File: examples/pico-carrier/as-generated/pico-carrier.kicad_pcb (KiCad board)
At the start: 2 copper layers, 82 x 68 mm, 9 parts, among them J1 5V IN, J3 GP0-GP15, J4 GP16-GP28, PWR, U1 Pico

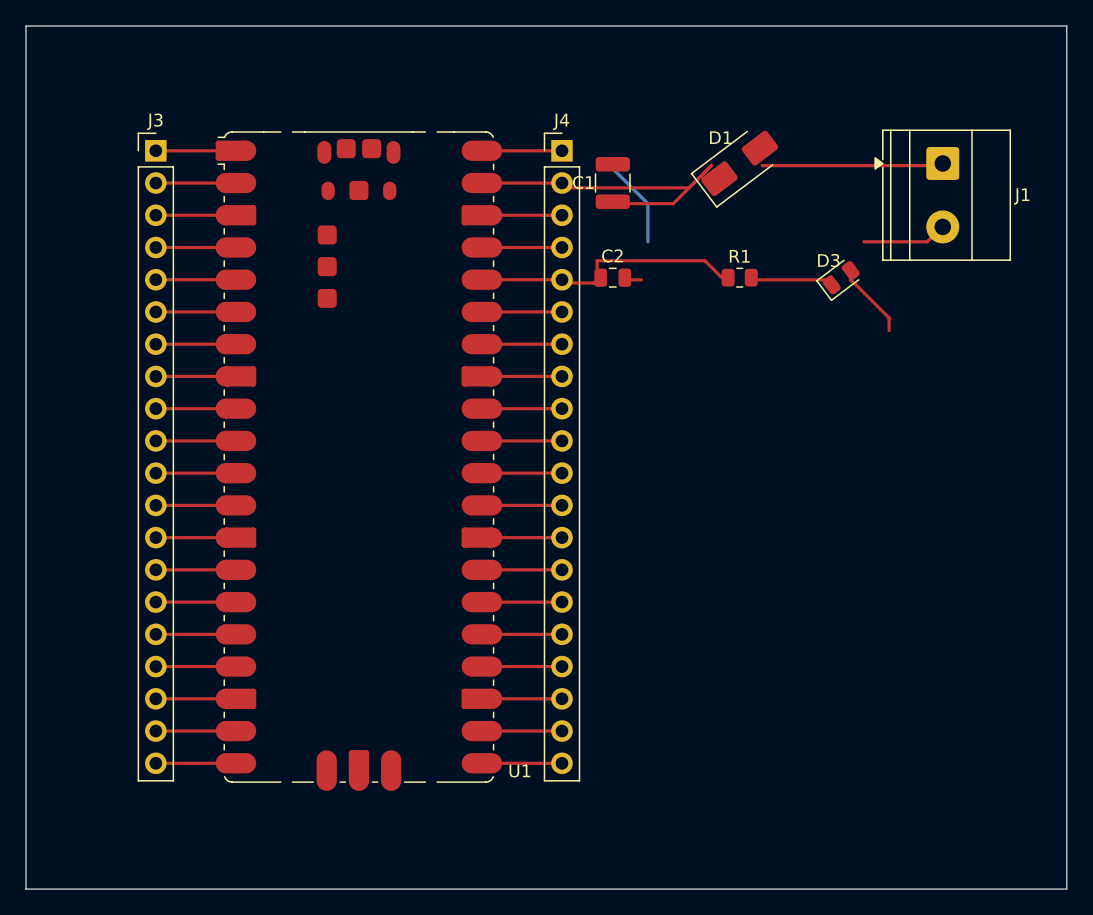
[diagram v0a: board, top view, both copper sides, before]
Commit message: Regenerate the five as round three drew them
All five reviewed projects pass their gates again: the buck all wire
with its feedback drawn home, the motor's logic named at the header,
the carrier reading as the pinout table it is - with its feed diode
finally pointing the right way - the filter compact with test points,
and the FPGA's capacitors sitting beside the units they feed. Thirty
renders redrawn, verdict tables at today's numbers.

Co-Authored-By: Claude Fable 5 <noreply@anthropic.com>
Claude-Session: https://claude.ai/code/session_01DUj7Ltu92tWg159mCSacwY
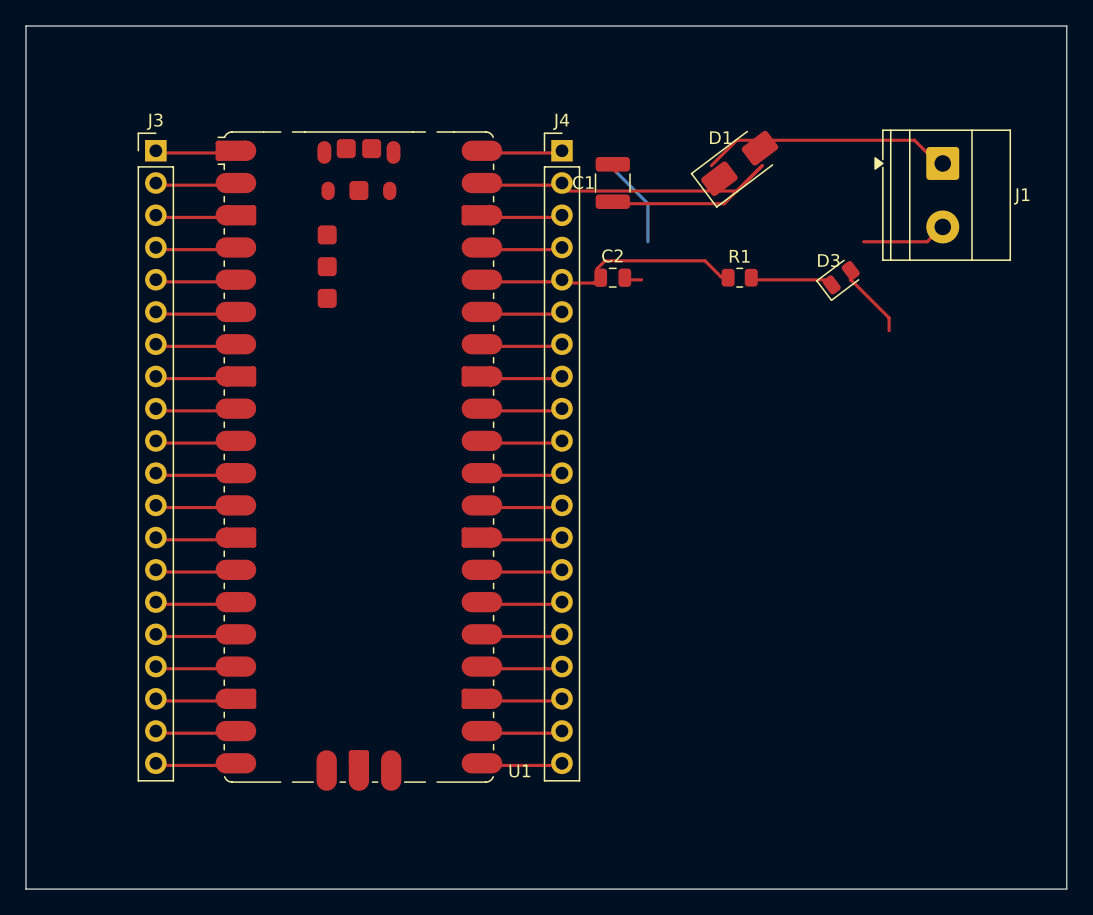
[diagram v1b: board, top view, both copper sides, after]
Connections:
- D1 pad 1: +5V -> /VSYS
- D1 pad 2: /VSYS -> +5V
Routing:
- net /VSYS: track 28.4 -> 36.6 mm
- net +5V: track 14.0 -> 19.7 mm

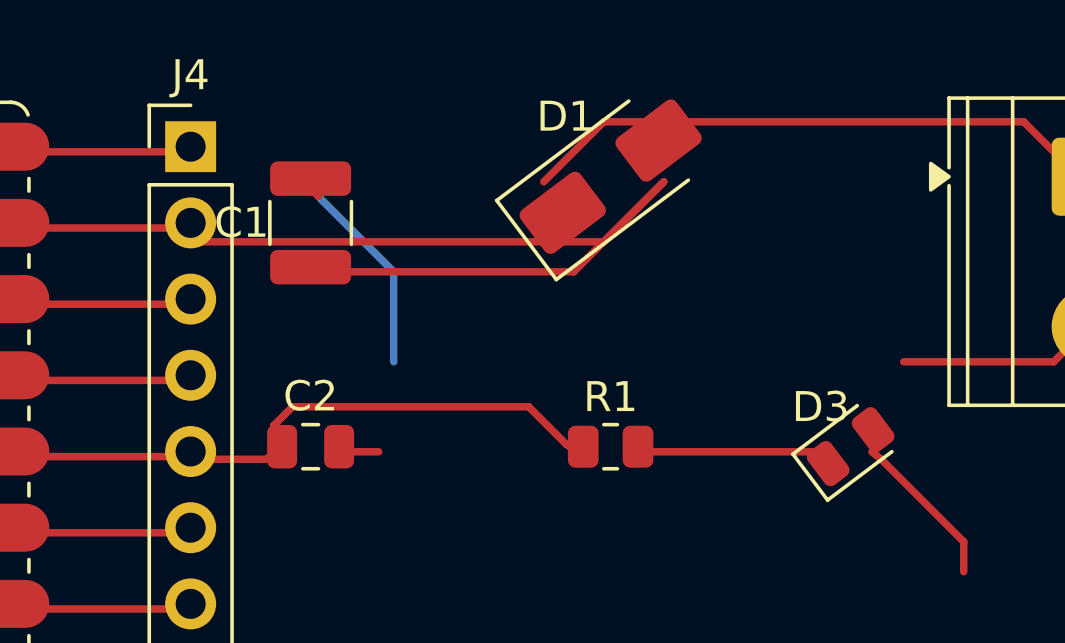
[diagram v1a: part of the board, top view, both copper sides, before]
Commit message: Regenerate the four boards whose corners were off the grid
Ninety-one bends at angles nobody chose, now none. All four still pass
their gates.

Co-Authored-By: Claude Fable 5 <noreply@anthropic.com>
Claude-Session: https://claude.ai/code/session_01DUj7Ltu92tWg159mCSacwY
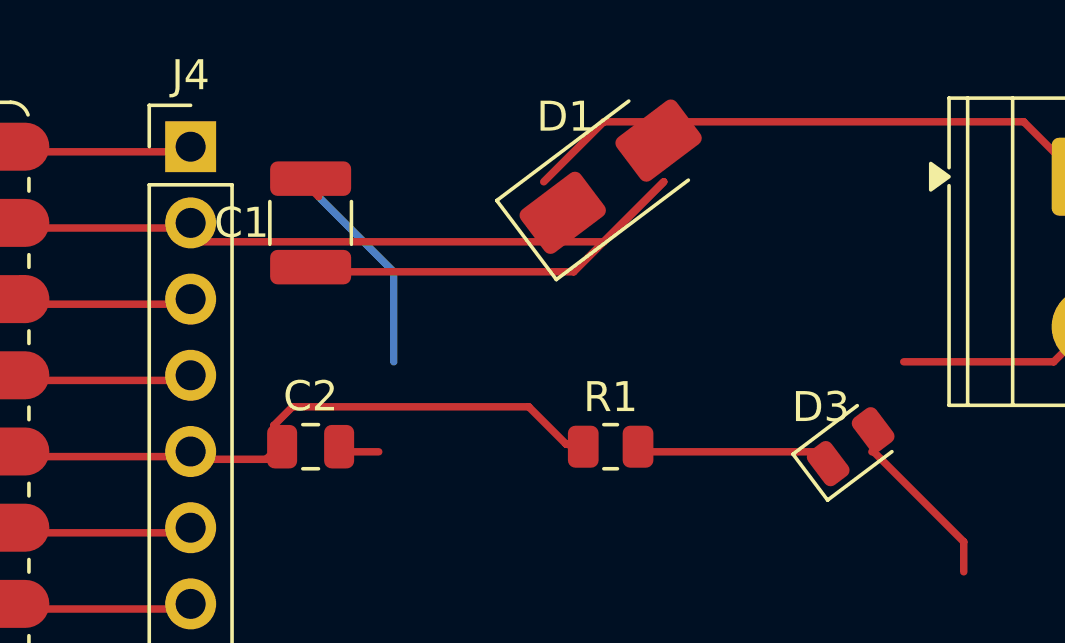
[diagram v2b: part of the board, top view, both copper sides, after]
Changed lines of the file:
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@@
 	(segment (start 156.0 73.0) (end 142.5 73.0) (width 0.25) (layer "F.Cu") (net 36))
 	(segment (start 142.5 73.0) (end 142.25 72.75) (width 0.25) (layer "F.Cu") (net 36))
-	(segment (start 142.25 72.75) (end 142.0 72.54) (width 0.25) (layer "F.Cu") (net 36))
-	(segment (start 146.0 74.015) (end 146.25 74.0) (width 0.25) (layer "F.Cu") (net 36))
+	(segment (start 142.25 72.75) (end 142.21 72.75) (width 0.25) (layer "F.Cu") (net 36))
+	(segment (start 142.21 72.75) (end 142.0 72.54) (width 0.25) (layer "F.Cu") (net 36))
+	(segment (start 146.0 74.015) (end 146.235 74.015) (width 0.25) (layer "F.Cu") (net 36))
+	(segment (start 146.235 74.015) (end 146.25 74.0) (width 0.25) (layer "F.Cu") (net 36))
 	(segment (start 146.25 74.0) (end 155.0 74.0) (width 0.25) (layer "F.Cu") (net 36))
 	(segment (start 155.0 74.0) (end 158.0 71.0) (width 0.25) (layer "F.Cu") (net 36))
-	(segment (start 145.05 80.0) (end 144.75 80.25) (width 0.25) (layer "F.Cu") (net 2))
+	(segment (start 145.05 80.0) (end 145.0 80.0) (width 0.25) (layer "F.Cu") (net 2))
+	(segment (start 145.0 80.0) (end 144.75 80.25) (width 0.25) (layer "F.Cu") (net 2))
 	(segment (start 144.75 80.25) (end 142.25 80.25) (width 0.25) (layer "F.Cu") (net 2))
-	(segment (start 142.25 80.25) (end 142.0 80.16) (width 0.25) (layer "F.Cu") (net 2))
-	(segment (start 145.05 80.0) (end 145.0 79.75) (width 0.25) (layer "F.Cu") (net 2))
+	(segment (start 142.25 80.25) (end 142.09 80.25) (width 0.25) (layer "F.Cu") (net 2))
+	(segment (start 142.09 80.25) (end 142.0 80.16) (width 0.25) (layer "F.Cu") (net 2))
+	(segment (start 145.05 80.0) (end 145.05 79.8) (width 0.25) (layer "F.Cu") (net 2))
+	(segment (start 145.05 79.8) (end 145.0 79.75) (width 0.25) (layer "F.Cu") (net 2))
 	(segment (start 145.0 79.75) (end 145.0 79.125) (width 0.25) (layer "F.Cu") (net 2))
 	(segment (start 145.0 79.125) (end 145.625 78.5) (width 0.25) (layer "F.Cu") (net 2))
 	(segment (start 145.625 78.5) (end 153.5 78.5) (width 0.25) (layer "F.Cu") (net 2))
 	(segment (start 153.5 78.5) (end 154.75 79.75) (width 0.25) (layer "F.Cu") (net 2))
-	(segment (start 154.75 79.75) (end 155.0875 80.0) (width 0.25) (layer "F.Cu") (net 2))
+	(segment (start 154.75 79.75) (end 154.8375 79.75) (width 0.25) (layer "F.Cu") (net 2))
+	(segment (start 154.8375 79.75) (end 155.0875 80.0) (width 0.25) (layer "F.Cu") (net 2))
 	(segment (start 156.9125 80.0) (end 163.0625 80.0) (width 0.25) (layer "F.Cu") (net 33))
-	(segment (start 146.0 71.065) (end 146.25 71.25) (width 0.25) (layer "F.Cu") (net 1))
+	(segment (start 146.0 71.065) (end 146.065 71.065) (width 0.25) (layer "F.Cu") (net 1))
+	(segment (start 146.065 71.065) (end 146.25 71.25) (width 0.25) (layer "F.Cu") (net 1))
 	(segment (start 146.25 71.25) (end 146.5 71.5) (width 0.25) (layer "F.Cu") (net 1))
 	(segment (start 146.5 71.5) (end 149.0 74.0) (width 0.25) (layer "B.Cu") (net 1))
 	(segment (start 149.0 74.0) (end 149.0 77.0) (width 0.25) (layer "B.Cu") (net 1))
 	(segment (start 146.95 80.0) (end 148.5 80.0) (width 0.25) (layer "F.Cu") (net 1))
-	(segment (start 164.9375 80.0) (end 165.25 80.25) (width 0.25) (layer "F.Cu") (net 1))
+	(segment (start 164.9375 80.0) (end 165.0 80.0) (width 0.25) (layer "F.Cu") (net 1))
+	(segment (start 165.0 80.0) (end 165.25 80.25) (width 0.25) (layer "F.Cu") (net 1))
 	(segment (start 165.25 80.25) (end 168.0 83.0) (width 0.25) (layer "F.Cu") (net 1))
 	(segment (start 168.0 83.0) (end 168.0 84.0) (width 0.25) (layer "F.Cu") (net 1))

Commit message: Regenerate the four the text and width work changed
Designators and values off the rails they were printed on, power-named
nets at the width their rule asks for, and the buck's feedback ending
on the capacitor pad it senses at.

Co-Authored-By: Claude Fable 5 <noreply@anthropic.com>
Claude-Session: https://claude.ai/code/session_01DUj7Ltu92tWg159mCSacwY
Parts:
- moved J3 6.00 mm to (110.2, 63.8)
- moved J4 6.00 mm to (142.2, 63.8)
- moved U1 6.00 mm to (126.2, 88.0)
- moved C1 3.00 mm to (146.2, 69.4)
- moved C2 3.00 mm to (146.2, 76.8)
- moved D1 3.00 mm to (156.2, 67.8)
- moved D3 3.00 mm to (164.2, 76.8)
- moved J1 3.00 mm to (172.2, 67.8)
- moved R1 3.00 mm to (156.2, 76.8)
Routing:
- net /VSYS: track 36.6 -> 33.6 mm
- net +3V3: track 21.4 -> 22.8 mm
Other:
- board size 82 x 68 mm -> 80 x 56 mm
